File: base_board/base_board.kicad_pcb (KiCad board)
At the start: 6 copper layers, 75 x 50 mm, 54 parts, among them J1 Conn_ARM_JTAG_SWD_20, J2 Conn_01x20_Pin, J3 Conn_01x20_Socket, SW1 SW_Push, U1 STM32F446ZEJx, U2 IS42S16400J-xT, U3 BMI270, U4 USB_C_Receptacle_USB2.0, U5 10p, U6 10p, U7 LD3985M33R_SOT23, Y1 Crystal_GND24

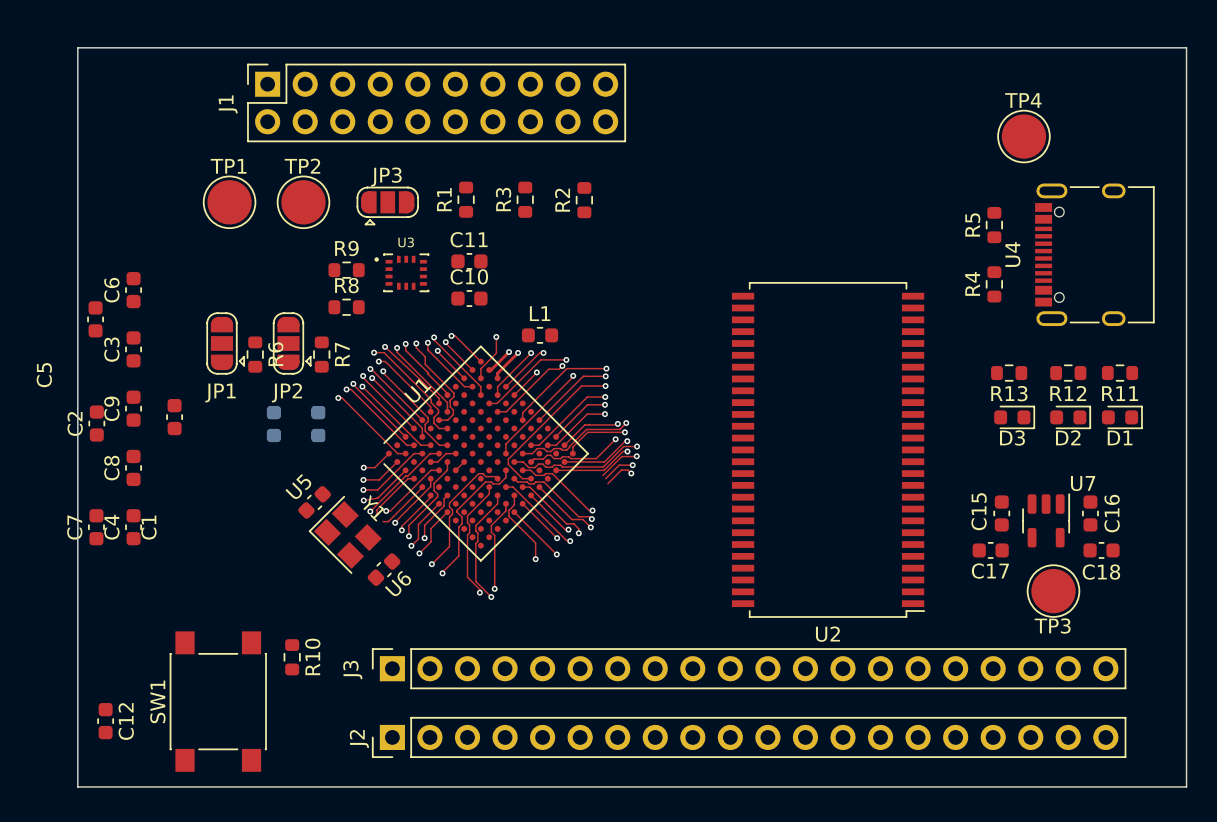
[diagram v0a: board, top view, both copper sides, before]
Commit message: [pcb] draft route of SDRAM
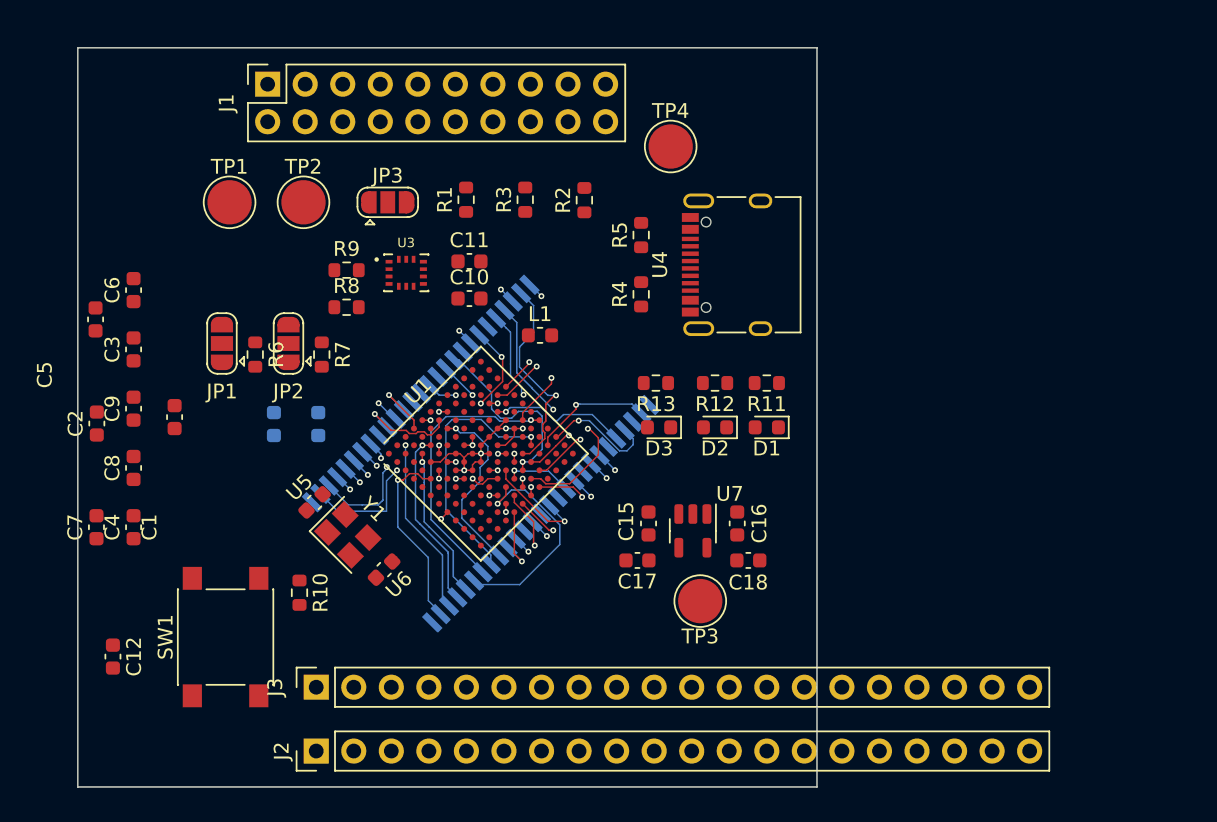
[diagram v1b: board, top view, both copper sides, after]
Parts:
- U2: moved to B.Cu
- moved C15 23.9 mm to (141.6, 100.2)
- moved C16 23.9 mm to (147.6, 100.2)
- moved C17 23.9 mm to (140.9, 102.7)
- moved C18 23.9 mm to (148.4, 102.7)
- moved D1 23.9 mm to (149.6, 93.7)
- moved D2 23.9 mm to (146.1, 93.7)
- moved D3 23.9 mm to (142.3, 93.7)
- moved R11 23.9 mm to (149.6, 90.7)
- moved R12 23.9 mm to (146.1, 90.7)
- moved R13 23.9 mm to (142.1, 90.7)
- moved R4 23.9 mm to (141.1, 84.7)
- moved R5 23.9 mm to (141.1, 80.7)
- moved TP3 23.9 mm to (145.1, 105.4)
- moved TP4 23.9 mm to (143.1, 74.7)
- moved U4 23.9 mm to (148.1, 82.7)
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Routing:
- net /FMC_D12: track 4.60 -> 19.9 mm, vias 1 -> 3
- net /FMC_A9: track 5.21 -> 19.4 mm, vias 1 -> 2
- net /FMC_BA1: track 5.71 -> 18.9 mm
- net /FMC_D13: track 2.83 -> 15.3 mm, vias 1 -> 2
- net /FMC_NBL0: track 4.95 -> 16.5 mm, vias 1 -> 2
- net /FMC_BA0: track 6.37 -> 17.6 mm
- net /FMC_D11: track 10.9 -> 21.7 mm, vias 1 -> 2
- net /FMC_SDCLK: track 7.40 -> 17.6 mm, vias 1 -> 2
- net +3.3V: track 2.73 -> 12.4 mm, vias 0 -> 3
- net /FMC_A10: track 5.87 -> 15.3 mm
- net /FMC_SDNCAS: track 5.73 -> 14.9 mm, vias 1 -> 2
- net /FMC_A2: track 6.27 -> 15.3 mm, vias 1 -> 2
- net /FMC_A3: track 3.98 -> 12.8 mm
- net /BOOT1: track 8.22 -> 0.00 mm, vias 1 -> 0
- net /FMC_D3: track 6.50 -> 14.1 mm, vias 1 -> 2
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- added copper zone on In1.Cu, net +3.3V
- added copper zone on In3.Cu, net GND
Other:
- board size 75 x 50 mm -> 50 x 50 mm

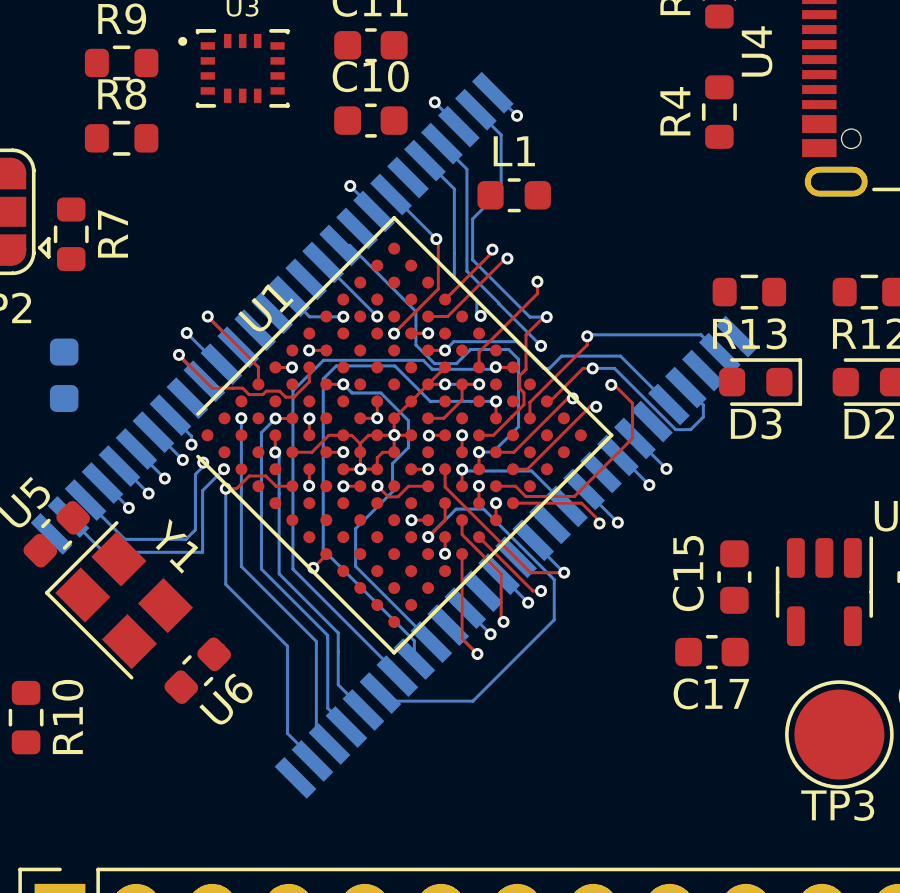
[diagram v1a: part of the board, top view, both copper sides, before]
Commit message: [pcb] corrected missed SDRAM trace
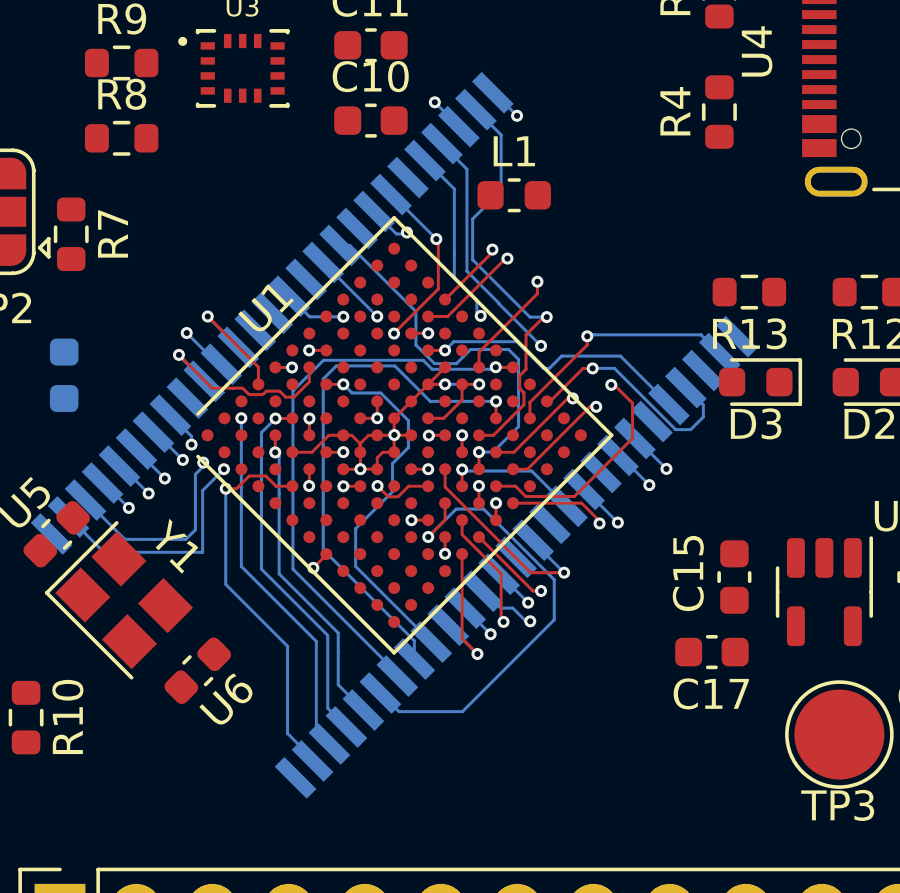
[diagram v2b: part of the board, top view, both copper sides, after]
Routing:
- net /FMC_SDNWE: track 9.49 -> 12.6 mm, vias 1 -> 2
- net /FMC_D11: track 21.7 -> 19.5 mm
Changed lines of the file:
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@@
   (segment (start 128.002258 99.437742) (end 127.57 99.87) (width 0.1) (layer "F.Cu") (net 112))
   (segment (start 128.002258 99.409798) (end 128.002258 99.437742) (width 0.1) (layer "F.Cu") (net 112))
+  (via (at 134.8 101.65) (size 0.4) (drill 0.2) (layers "F.Cu" "B.Cu") (net 112))
   (via (at 127.57 99.87) (size 0.4) (drill 0.2) (layers "F.Cu" "B.Cu") (net 112))
   (segment (start 131.99 103.82) (end 131.47 103.82) (width 0.1) (layer "In2.Cu") (net 112))
   (segment (start 132.59 103.22) (end 131.99 103.82) (width 0.1) (layer "In2.Cu") (net 112))
+  (segment (start 134.8 101.77) (end 134.8 101.65) (width 0.1) (layer "In2.Cu") (net 112))
   (segment (start 134.14 102.43) (end 133.35 103.22) (width 0.1) (layer "In2.Cu") (net 112))
   (segment (start 133.35 103.22) (end 132.59 103.22) (width 0.1) (layer "In2.Cu") (net 112))
+  (segment (start 134.14 102.43) (end 134.8 101.77) (width 0.1) (layer "In2.Cu") (net 112))
   (segment (start 131.47 103.77) (end 127.57 99.87) (width 0.1) (layer "In2.Cu") (net 112))
   (segment (start 131.47 103.82) (end 131.47 103.77) (width 0.1) (layer "In2.Cu") (net 112))
+  (segment (start 133.247235 100.647235) (end 133.81 101.21) (width 0.1) (layer "B.Cu") (net 112))
+  (segment (start 133.81 101.21) (end 134.22 101.21) (width 0.1) (layer "B.Cu") (net 112))
+  (segment (start 134.66 101.65) (end 134.8 101.65) (width 0.1) (layer "B.Cu") (net 112))
+  (segment (start 133.199493 100.647235) (end 133.247235 100.647235) (width 0.1) (layer "B.Cu") (net 112))
   (segment (start 133.199493 100.647235) (end 133.199493 100.689493) (width 0.1) (layer "B.Cu") (net 112))
+  (segment (start 134.22 101.21) (end 134.66 101.65) (width 0.1) (layer "B.Cu") (net 112))
   (segment (start 131.43 95.45) (end 131.42 95.46) (width 0.1) (layer "F.Cu") (net 113))
   (segment (start 131.962056 95.45) (end 131.43 95.45) (width 0.1) (layer "F.Cu") (net 113))
@@
   (segment (start 131.4 98.84) (end 131.962056 98.277944) (width 0.1) (layer "F.Cu") (net 121))
   (via (at 131.4 98.84) (size 0.4) (drill 0.2) (layers "F.Cu" "B.Cu") (net 121))
+  (segment (start 133.246846 97.91) (end 132.33 97.91) (width 0.1) (layer "B.Cu") (net 121))
   (segment (start 132.33 97.91) (end 131.4 98.84) (width 0.1) (layer "B.Cu") (net 121))
-  (segment (start 132.888545 104.311455) (end 135.6 101.6) (width 0.1) (layer "B.Cu") (net 121))
+  (segment (start 130.424034 104.66) (end 132.54 104.66) (width 0.1) (layer "B.Cu") (net 121))
   (segment (start 135.6 100.263154) (end 133.246846 97.91) (width 0.1) (layer "B.Cu") (net 121))
-  (segment (start 130.075489 104.311455) (end 132.888545 104.311455) (width 0.1) (layer "B.Cu") (net 121))
+  (segment (start 132.54 104.66) (end 135.6 101.6) (width 0.1) (layer "B.Cu") (net 121))
   (segment (start 135.6 101.6) (end 135.6 100.263154) (width 0.1) (layer "B.Cu") (net 121))
-  (segment (start 133.246846 97.91) (end 132.33 97.91) (width 0.1) (layer "B.Cu") (net 121))
-  (segment (start 129.805381 104.041347) (end 130.075489 104.311455) (width 0.1) (layer "B.Cu") (net 121))
+  (segment (start 129.805381 104.041347) (end 130.424034 104.66) (width 0.1) (layer "B.Cu") (net 121))
   (segment (start 132.527742 97.147056) (end 132.527742 96.592258) (width 0.1) (layer "F.Cu") (net 122))
   (segment (start 132.527742 96.592258) (end 132.53 96.59) (width 0.1) (layer "F.Cu") (net 122))
@@
   (segment (start 138.21 94.38) (end 137.6 93.77) (width 0.1) (layer "F.Cu") (net 130))
   (segment (start 136.27 97.49) (end 136.44 97.32) (width 0.1) (layer "F.Cu") (net 130))
-  (via (at 128.8 87.14) (size 0.4) (drill 0.2) (layers "F.Cu" "B.Cu") (net 130))
+  (via (at 130.69 88.69) (size 0.4) (drill 0.2) (layers "F.Cu" "B.Cu") (net 130))
   (via (at 137.5 93.77) (size 0.4) (drill 0.2) (layers "F.Cu" "B.Cu") (net 130))
+  (segment (start 135.9787 90.5787) (end 135.32 89.92) (width 0.1) (layer "In2.Cu") (net 130))
+  (segment (start 137.17 92.86) (end 137.17 91.23) (width 0.1) (layer "In2.Cu") (net 130))
   (segment (start 137.5 93.77) (end 137.5 93.19) (width 0.1) (layer "In2.Cu") (net 130))
-  (segment (start 135.9787 90.5787) (end 133.9 88.5) (width 0.1) (layer "In2.Cu") (net 130))
-  (segment (start 130.16 88.5) (end 128.8 87.14) (width 0.1) (layer "In2.Cu") (net 130))
+  (segment (start 137.5 93.19) (end 137.17 92.86) (width 0.1) (layer "In2.Cu") (net 130))
+  (segment (start 135.32 89.92) (end 134.26 89.92) (width 0.1) (layer "In2.Cu") (net 130))
+  (segment (start 132.02 90.02) (end 130.69 88.69) (width 0.1) (layer "In2.Cu") (net 130))
+  (segment (start 137.17 91.23) (end 136.5187 90.5787) (width 0.1) (layer "In2.Cu") (net 130))
+  (segment (start 134.26 89.92) (end 134.16 90.02) (width 0.1) (layer "In2.Cu") (net 130))
   (segment (start 136.5187 90.5787) (end 135.9787 90.5787) (width 0.1) (layer "In2.Cu") (net 130))
-  (segment (start 137.5 93.19) (end 137.17 92.86) (width 0.1) (layer "In2.Cu") (net 130))
-  (segment (start 128.72 87.14) (end 128.8 87.14) (width 0.1) (layer "In2.Cu") (net 130))
-  (segment (start 133.9 88.5) (end 130.16 88.5) (width 0.1) (layer "In2.Cu") (net 130))
-  (segment (start 137.17 91.23) (end 136.5187 90.5787) (width 0.1) (layer "In2.Cu") (net 130))
-  (segment (start 137.17 92.86) (end 137.17 91.23) (width 0.1) (layer "In2.Cu") (net 130))
+  (segment (start 134.16 90.02) (end 132.02 90.02) (width 0.1) (layer "In2.Cu") (net 130))
   (segment (start 129.593249 87.933249) (end 129.593249 87.990023) (width 0.1) (layer "B.Cu") (net 130))
-  (segment (start 128.8 87.14) (end 129.593249 87.933249) (width 0.1) (layer "B.Cu") (net 130))
+  (segment (start 129.593249 87.993249) (end 130.34 88.74) (width 0.1) (layer "B.Cu") (net 130))
+  (segment (start 130.64 88.74) (end 130.34 88.74) (width 0.1) (layer "B.Cu") (net 130))
+  (segment (start 130.69 88.69) (end 130.64 88.74) (width 0.1) (layer "B.Cu") (net 130))
+  (segment (start 129.593249 87.990023) (end 129.593249 87.993249) (width 0.1) (layer "B.Cu") (net 130))
   (segment (start 136.787001 94.5) (end 137 94.5) (width 0.1) (layer "F.Cu") (net 131))
   (segment (start 134.224798 96.581371) (end 134.70563 96.581371) (width 0.1) (layer "F.Cu") (net 131))

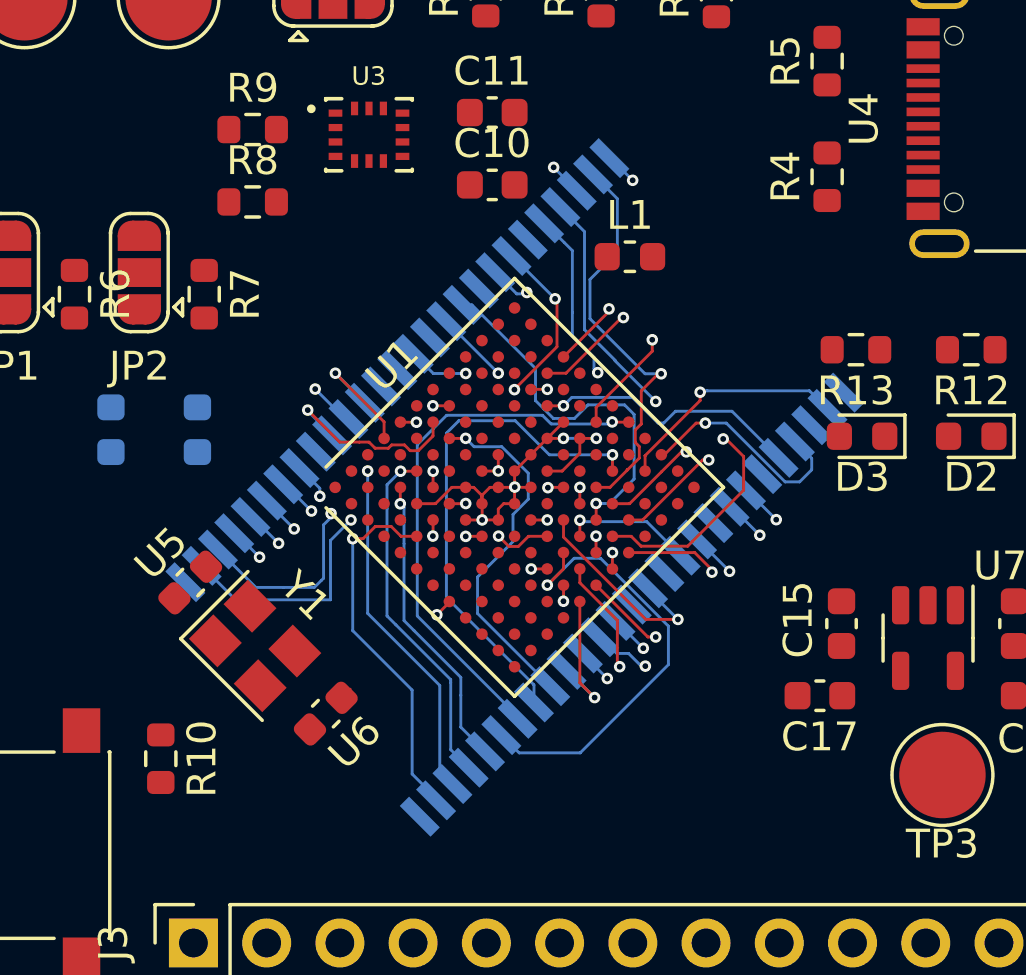
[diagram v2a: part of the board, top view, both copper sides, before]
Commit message: [pcb] draft length match for SDRAM
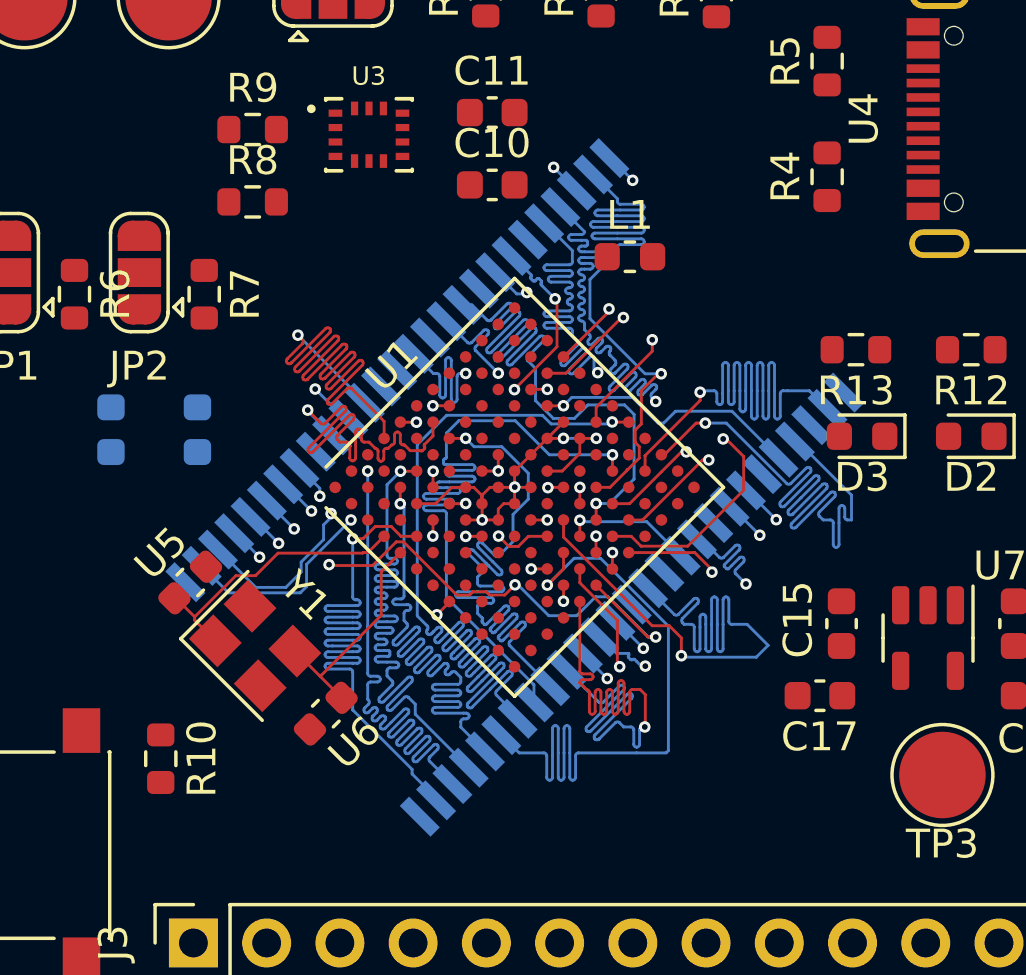
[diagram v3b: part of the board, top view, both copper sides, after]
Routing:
- net /FMC_NBL1: track 4.41 -> 26.2 mm
- net /FMC_SDNRAS: track 4.91 -> 26.1 mm
- net /FMC_D7: track 7.25 -> 26.2 mm
- net /FMC_D1: track 7.91 -> 26.2 mm
- net /FMC_D5: track 8.14 -> 26.1 mm
- net /FMC_D0: track 8.23 -> 26.2 mm
- net /FMC_D9: track 8.25 -> 26.1 mm
- net /FMC_BA1: track 18.9 -> 36.6 mm
- net /FMC_D11: track 19.5 -> 36.9 mm
- net /FMC_D4: track 9.53 -> 26.1 mm
- net /FMC_A8: track 4.18 -> 20.0 mm, vias 2 -> 4
- net /FMC_A0: track 10.4 -> 26.1 mm
- net /FMC_A7: track 11.0 -> 26.1 mm
- net /FMC_A9: track 19.4 -> 34.4 mm
- net /FMC_D8: track 8.13 -> 22.1 mm
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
